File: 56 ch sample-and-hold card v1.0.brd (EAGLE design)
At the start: 170.8 x 36.2 mm, 127 parts, among them IC1 74HCT4051D, IC10 TL074JT, IC11 74HCT4051D, IC12 TL074JT, IC13 TL074JT, IC14 74HCT4051D, IC15 TL074JT, IC16 TL074JT, IC17 74HCT4051D, IC18 TL074JT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

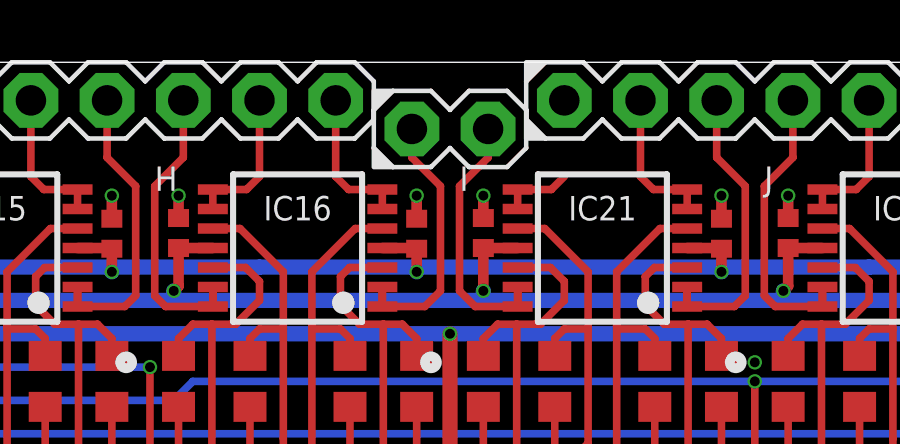
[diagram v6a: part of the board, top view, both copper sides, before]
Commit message: Switched to 2p nude
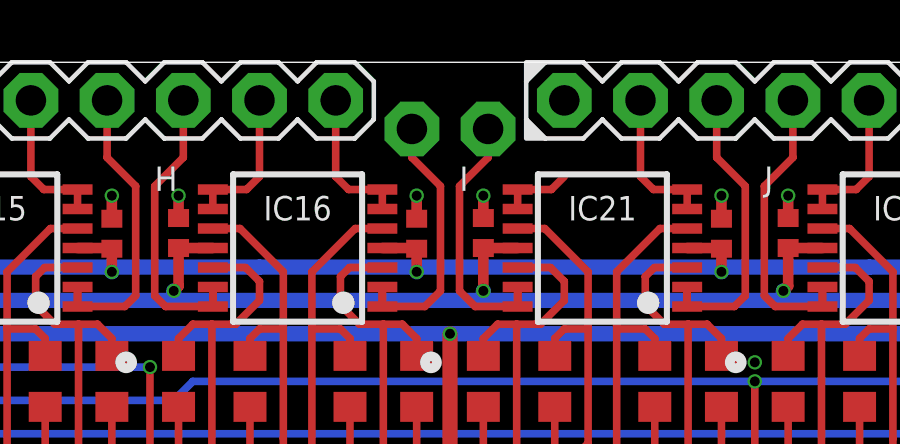
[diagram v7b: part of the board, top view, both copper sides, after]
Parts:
- X9: device joakim:MA02-1J -> joakim:MA02N-1J
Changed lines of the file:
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@@
 <attribute name="VALUE" x="128.5875" y="31.0515" size="1.27" layer="27" ratio="10"/>
 </element>
-<element name="X9" library="joakim" package="MA02-1J" value="DNM" x="110.8075" y="33.9725" smashed="yes">
+<element name="X9" library="joakim" package="MA02N-1J" value="DNM" x="110.8075" y="33.9725" smashed="yes">
 <attribute name="VALUE" x="106.9975" y="31.0515" size="1.27" layer="27" ratio="10"/>
 </element>

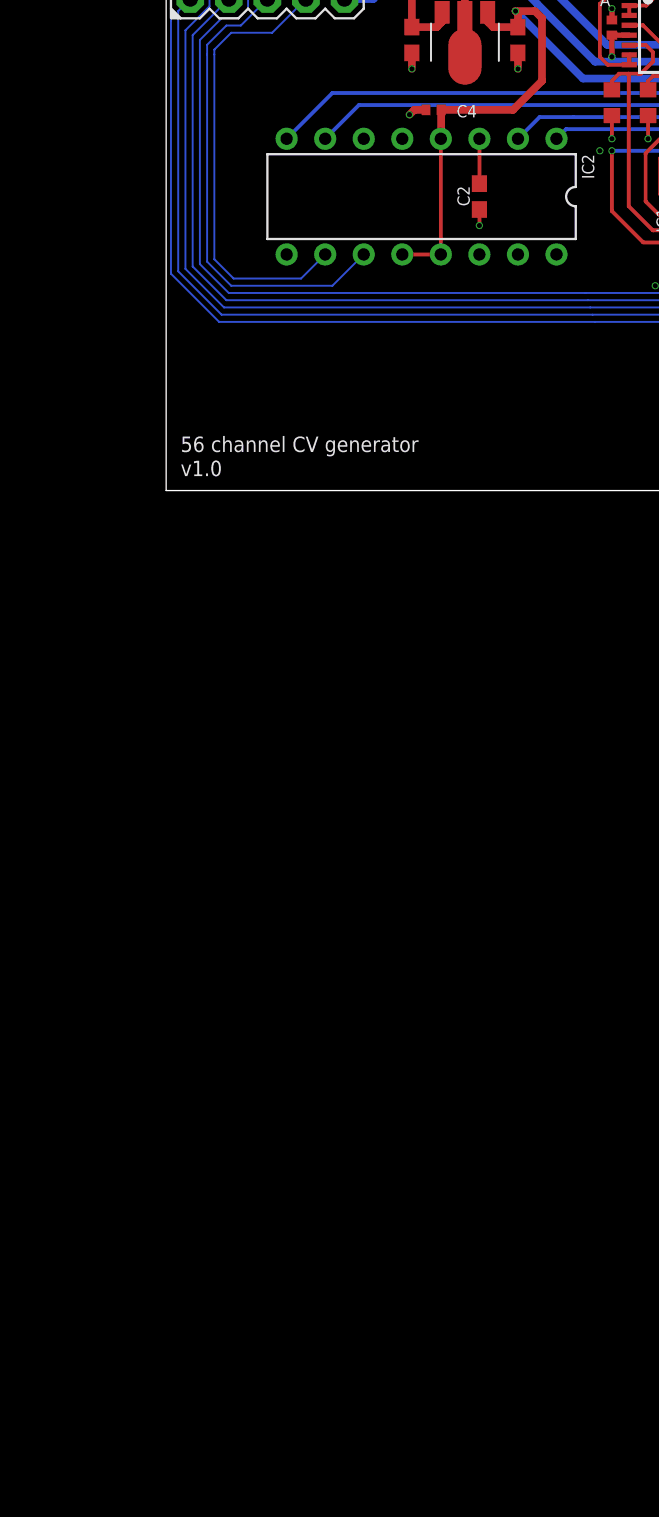
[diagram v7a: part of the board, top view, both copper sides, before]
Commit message: Switched to internal reference and buffering
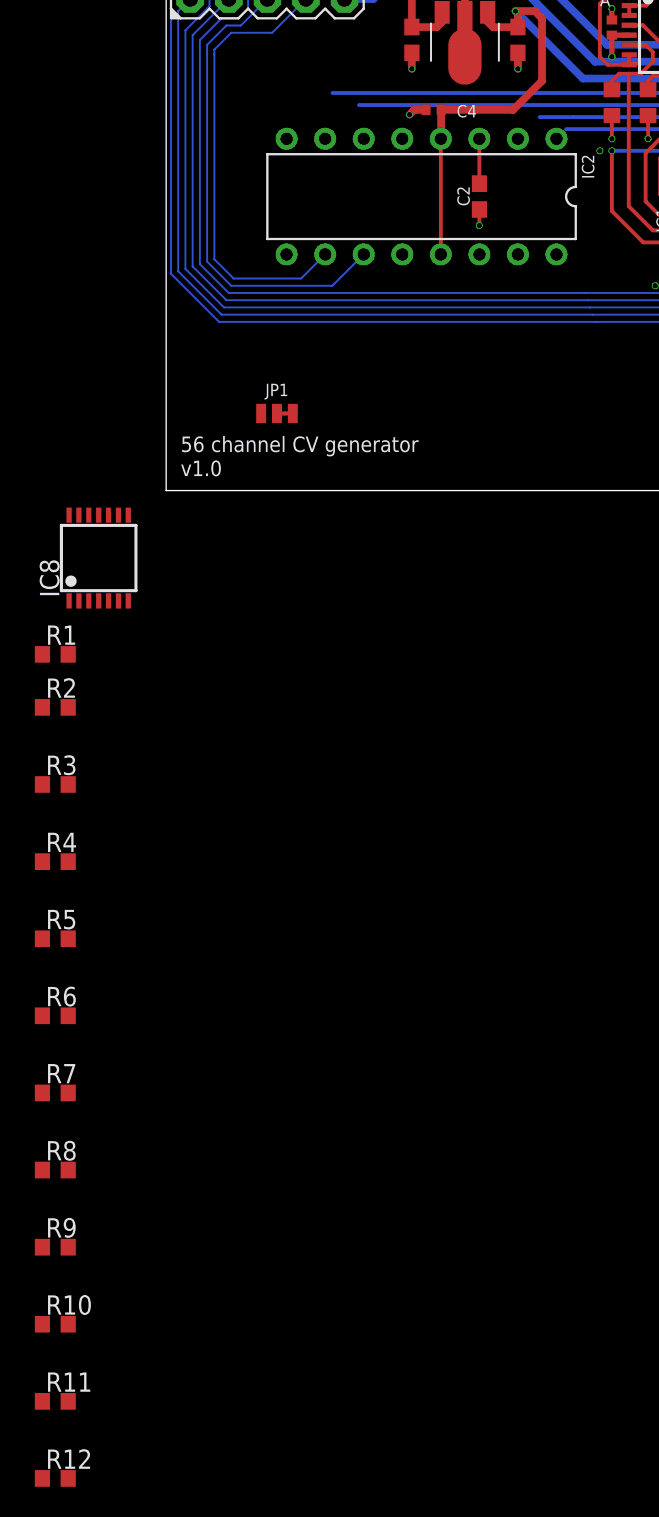
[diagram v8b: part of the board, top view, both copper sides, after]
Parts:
- added IC8: TL074JT, joakim:TSSOP14J
- added JP1: JUMPER-SMT_3_1-NC_TRACE_NO-SILK_DNM, SparkFun-Jumpers:SMT-JUMPER_3_1-NC_TRACE_NO-SILK
- added R1, R2, R3, R4, R5, R6, R7, R8: 10k, rcl:R0603
- added R10, R11, R12, R9: 220R, rcl:R0603
- C4: value (none) -> 1uF
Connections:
- net N$8 renamed 5V_REF
- new net !SYNC: IC2.9
- new net +3V3: JP1.1
- new net DAC_BUF_1: IC8.1, R1.2, R9.1
- new net DAC_BUF_2: IC8.7, R10.1, R4.2
- new net DAC_BUF_3: IC8.8, R11.1, R6.2
- new net DAC_BUF_4: IC8.14, R12.1, R8.2
- new net DAC_RAW_1: IC2.1, IC8.3
- new net DAC_RAW_2: IC2.2, IC8.5
- new net DAC_RAW_3: IC2.7, IC8.10
- new net DAC_RAW_4: IC2.8, IC8.12
- new net N$1: IC2.12, JP1.2
- new net N$2: IC8.2
- new net N$3: IC8.6, R3.2, R4.1
- new net N$4: IC8.9, R5.2, R6.1
- new net N$5: IC8.13, R7.2, R8.1
- new net N$6: R1.1, R2.2
- new net V+: IC8.4
- new net V-: IC8.11
- net +5V: now also JP1.3; no longer IC2.12
- net AGND: now also R2.1, R3.1, R5.1, R7.1; no longer IC2.9
- net DAC_1: now also R9.2; no longer IC2.1
- net DAC_2: now also R10.2; no longer IC2.2
- net DAC_3: now also R11.2; no longer IC2.7
- net DAC_4: now also R12.2; no longer IC2.8
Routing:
- net DAC_4: track 65.2 -> 60.9 mm
- net DAC_3: track 103.5 -> 100.4 mm
- net +5V: track 286.2 -> 283.7 mm
- net DAC_2: track 129.9 -> 127.9 mm
- net DAC_1: track 139.2 -> 138.3 mm
